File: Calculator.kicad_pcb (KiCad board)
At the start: 6 copper layers, 69.9 x 153.8 mm, 7 parts, among them U1 STM32F205VGTx

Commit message: Added SWL
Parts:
- added C7: 4.7µF, Capacitor_SMD:C_0603_1608Metric_Pad1.08x0.95mm_HandSolder, F.Cu at (68.3, 44.1)
- added J1: Conn_01x05, Connector_PinHeader_2.54mm:PinHeader_1x05_P2.54mm_Vertical, F.Cu at (126.7, 43.8)
- added TP1: NRST, TestPoint:TestPoint_Pad_D1.0mm, B.Cu at (69.5, 49.5)
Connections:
- C6 pad 1: Vdd -> Vss
- C6 pad 2: Vss -> Vdd
- U1 pad 14: unconnected-(U1-NRST-Pad14) -> NRST
- U1 pad 20: unconnected-(U1-VSSA-Pad20) -> Vss
- U1 pad 21: unconnected-(U1-VREF+-Pad21) -> Vdd
- U1 pad 22: unconnected-(U1-VDDA-Pad22) -> Vdd
- U1 pad 6: unconnected-(U1-VBAT-Pad6) -> Vdd
- U1 pad 72: unconnected-(U1-PA13-Pad72) -> SWDIO
- U1 pad 76: unconnected-(U1-PA14-Pad76) -> SWCLK
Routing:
- net NRST: track 0.00 -> 60.6 mm, vias 0 -> 1
- net SWCLK: track 0.00 -> 38.1 mm, vias 0 -> 1
- net SWDIO: track 0.00 -> 34.7 mm
- net Vdd: track 15.5 -> 21.0 mm, vias 10 -> 14
- net Vss: track 11.5 -> 13.1 mm, vias 7 -> 8
- added copper zone on In3.Cu, net Vss

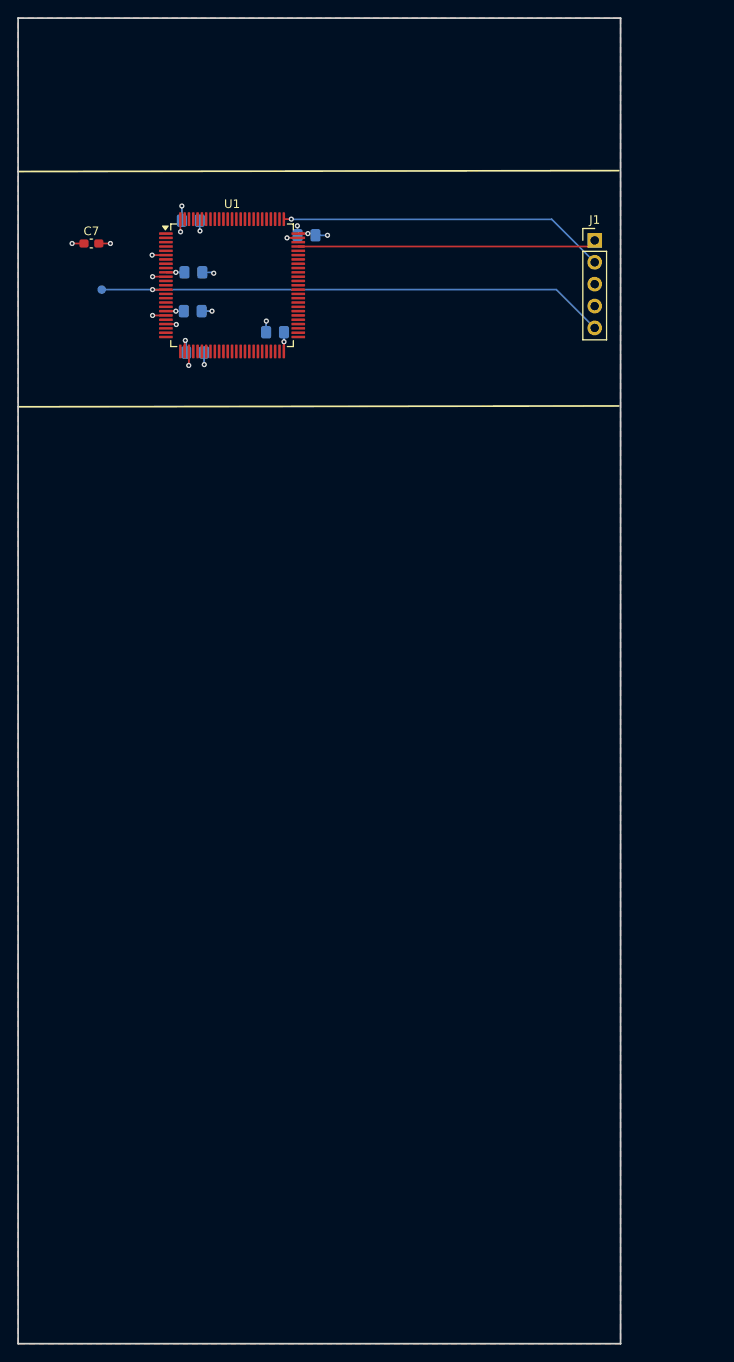
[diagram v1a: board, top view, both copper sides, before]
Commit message: Added Display and Batteries
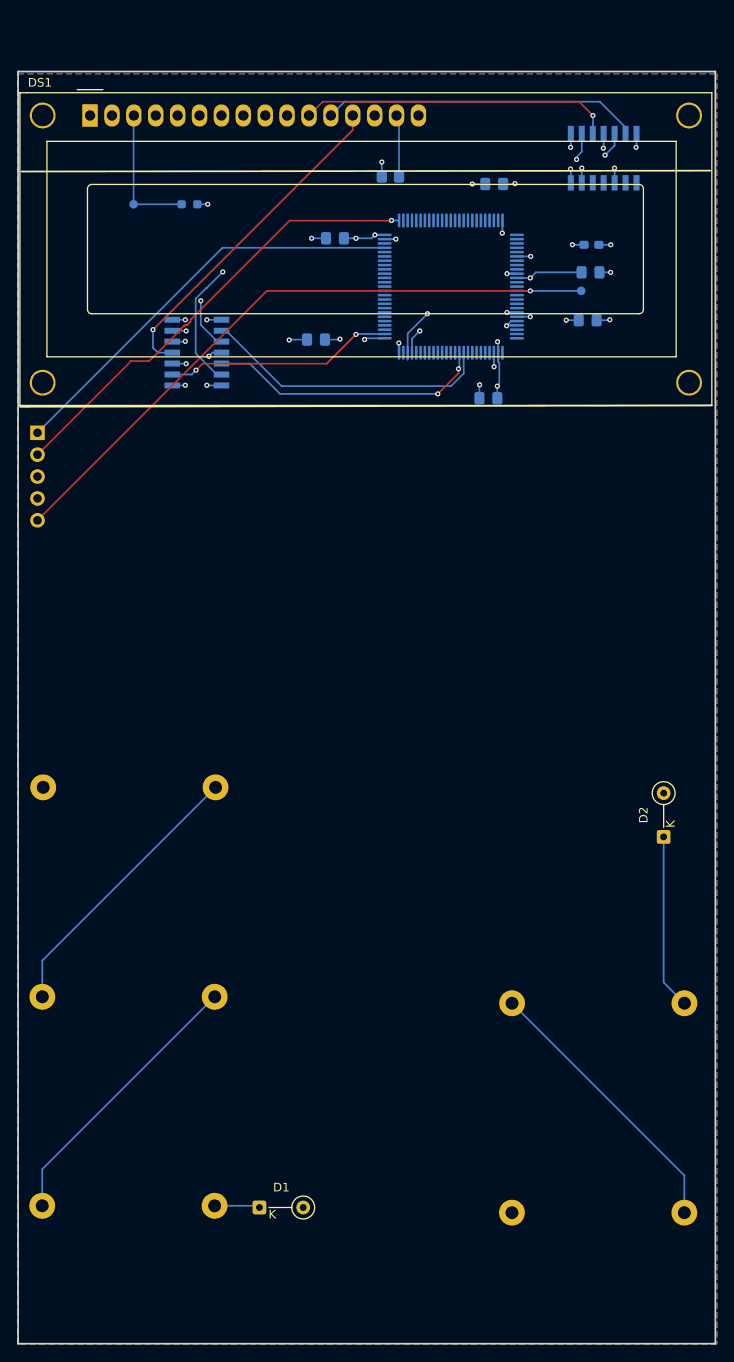
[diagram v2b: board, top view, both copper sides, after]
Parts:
- added Buffer1: ~, Texas Instruments Logic Footprints:SNx4HCT125, B.Cu at (80.5, 56.8)
- added Buffer2: ~, Texas Instruments Logic Footprints:SNx4HCT125, B.Cu at (127.7, 34.3)
- added D1: D, Diode_THT:D_DO-35_SOD27_P5.08mm_Vertical_KathodeUp, F.Cu at (87.8, 156.0)
- added D2: D, Diode_THT:D_DO-35_SOD27_P5.08mm_Vertical_KathodeUp, F.Cu at (134.7, 113.0)
- added DS1: WC1602A, Display:WC1602A, F.Cu at (68.2, 29.3)
- added R1: 50Ω, Resistor_SMD:R_0805_2012Metric_Pad1.20x1.40mm_HandSolder, B.Cu at (103.0, 36.4)
- added R2: 1.8kΩ, Resistor_SMD:R_0603_1608Metric_Pad0.98x0.95mm_HandSolder, B.Cu at (79.7, 39.6)
- added TP2: TestPoint, TestPoint:TestPoint_Pad_D1.0mm, B.Cu at (73.2, 39.6)
- added U2: ~, CalcLibrary:BH-25C-1, B.Cu at (128.6, 156.6)
- added U3: ~, CalcLibrary:BH-25C-1, B.Cu at (128.6, 132.3)
- added U4: ~, CalcLibrary:BH-25C-1, B.Cu at (74.2, 107.2)
- added U5: ~, CalcLibrary:BH-25C-1, B.Cu at (74.1, 131.6)
- added U6: ~, CalcLibrary:BH-25C-1, B.Cu at (74.1, 155.8)
- C7, J1, U1: moved to B.Cu
- moved J1 68.4 mm to (62.0, 66.1), turned to 180 degrees
- moved C7 58.0 mm to (126.3, 44.3), turned to 180 degrees
- moved TP1 55.6 mm to (125.1, 49.6)
- moved C3 46.1 mm to (126.2, 47.5), turned to 0 degrees
- moved C4 45.8 mm to (125.9, 53.0)
- moved C2 35.5 mm to (115.0, 37.2)
- moved C5 34.4 mm to (114.4, 62.1), turned to 0 degrees
- moved U1 25.4 mm to (110.0, 49.1), turned to 180 degrees
- moved C6 4.83 mm to (94.4, 55.3)
- moved C1 3.32 mm to (96.6, 43.5)
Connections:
- net Vdd renamed VDD
- net Vss renamed VSS
- U1 pad 35: unconnected-(U1-PB0-Pad35) -> DS_RS_3V3
- U1 pad 36: unconnected-(U1-PB1-Pad36) -> DS_E_3V3
- U1 pad 47: unconnected-(U1-PB10-Pad47) -> DS_D4_3V3
- U1 pad 48: unconnected-(U1-PB11-Pad48) -> DS_D5_3V3
- U1 pad 51: unconnected-(U1-PB12-Pad51) -> DS_D6_3V3
- U1 pad 52: unconnected-(U1-PB13-Pad52) -> DS_D7_3V3
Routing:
- net DS_D7_5V: track 0.00 -> 43.0 mm, vias 0 -> 1
- net DS_D6_5V: track 0.00 -> 39.0 mm, vias 0 -> 1
- net DS_D5_3V3: track 0.00 -> 37.5 mm, vias 0 -> 2
- net DS_D5_5V: track 0.00 -> 36.8 mm
- net DS_D4_5V: track 0.00 -> 36.4 mm, vias 0 -> 1
- net DS_E_5V: track 0.00 -> 34.4 mm, vias 0 -> 1
- net DS_RS_3V3: track 0.00 -> 33.8 mm
- net DS_D4_3V3: track 0.00 -> 33.6 mm, vias 0 -> 2
- net Net-(U4--): track 0.00 -> 32.6 mm
- net Net-(U2--): track 0.00 -> 32.6 mm
- net Net-(U5--): track 0.00 -> 32.5 mm
- net DS_E_3V3: track 0.00 -> 32.4 mm, vias 0 -> 2
- net DS_RS_5V: track 0.00 -> 29.7 mm, vias 0 -> 1
- net DS_D7_3V3: track 0.00 -> 26.7 mm, vias 0 -> 2
- net DS_D6_3V3: track 0.00 -> 25.2 mm, vias 0 -> 2
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- added copper zone on In4.Cu, net 5V
- removed copper zone on In4.Cu, net (none)
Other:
- board size 69.9 x 153.8 mm -> 80.9 x 147.6 mm
